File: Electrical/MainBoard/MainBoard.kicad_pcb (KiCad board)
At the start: 4 copper layers, 100 x 100 mm, 147 parts, among them J1 SNAP Program, J10 Refl_Mount, J11 Refl_Mount, J12 Refl_PCB_Connect, J13 Refl_PCB_Connect, J14 Refl_PCB_Connect, J15 USB_B_Micro, J16 MEM2061-01-188-00-A, J17 GPIO, J2 UART Connect, J3 SPI/I2C Connect, J4 5V Supply, J5 3.3V Supply, J6 USB_B_Micro, J7 Battery1, J8 Battery1, J9 Refl_Mount, K1 QRE1113GR, K2 QRE1113GR, K3 QRE1113GR, M1 Motor_DC, M2 Motor_DC, SW1 Reset, SW10 User_Button, SW2 5V Bypass, SW3 All Power Switch, SW4 SW_SPST, SW5 SW_SPST, SW6 SW_SPST, SW7 SW_SPST, SW8 User_Button, SW9 User_Button, U1 PIC32MZ2048EFH144-I/PL, U10 MCP2221A-I_SL, U11 M95M01-DFMN6TP, U12 DRV8842PWPR, U13 Quad_Encoder, U14 Quad_Encoder, U15 DRV8842PWPR, U2 GSF7002DW, U3 GSF7002DW, U4 GSF7002DW, U5 AP2114HA-3.3TRG1, U6 ICM-42688-P, U7 MAX-M8C-0, U8 GSF7002DW, U9 AP2114HA-3.3TRG1

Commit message: Begin layout of pcb
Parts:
- added E1: APAE1590R2540AKDB1-T, RobotLibrary:XDCR_APAE1590R2540AKDB1-T, F.Cu at (132.5, 86.4)
- C13: value 10 uF -> 4.7 uF; footprint Capacitor_THT:CP_Radial_Tantal_D5.0mm_P2.50mm -> Capacitor_SMD:C_0805_2012Metric_Pad1.18x1.45mm_HandSolder
- C14: value 0.1 uF -> 4.7 uF
- C15: value 2.2 uF -> 10 uF; footprint Capacitor_SMD:C_0805_2012Metric_Pad1.18x1.45mm_HandSolder -> Capacitor_THT:CP_Radial_Tantal_D5.0mm_P2.50mm
- C18: value 4.7 uF -> 2.2 uF
- C19: value 4.7 uF -> 0.1 uF
- C20, C26: value 0.1 uF -> 0.47 uF
- C21, C29: value 0.1 uF -> 0.01 uF
- C23, C31: value 0.47 uF -> 0.1 uF
- C24, C32: value 0.01 uF -> 0.1 uF
- C25, C33: value 0.1 uF -> 100 uF; footprint Capacitor_SMD:C_0805_2012Metric_Pad1.18x1.45mm_HandSolder -> RobotLibrary:PCAP_8x10-ELECT_NCA-M
- C28, C36: value 100 uF -> 0.1 uF; footprint RobotLibrary:PCAP_8x10-ELECT_NCA-M -> Capacitor_SMD:C_0805_2012Metric_Pad1.18x1.45mm_HandSolder
- D1: value LED 2 -> ON
- D2: value LED 1 -> LED 2
- D3: value LED 4 -> LED 1
- D4: value LED 3 -> LED 4
- D5: value LED 6 -> LED 3
- D6: value LED 5 -> LED 6
- D7: value ON -> LED 5
- J12: value Refl_PCB_Connect -> Refl_Mount; footprint RobotLibrary:CONN3_22232031_MOL -> Connector_PinHeader_2.54mm:PinHeader_2x02_P2.54mm_Vertical
- J15: value USB_B_Micro -> Refl_PCB_Connect; footprint RobotLibrary:AMPHENOL_10118193-0001LF -> RobotLibrary:CONN3_22232031_MOL
- J16: value MEM2061-01-188-00-A -> GPIO; footprint RobotLibrary:MEM2061-01-188-00-A_GCT -> Connector_PinHeader_2.54mm:PinHeader_2x10_P2.54mm_Vertical
- J17: value GPIO -> MEM2061-01-188-00-A; footprint Connector_PinHeader_2.54mm:PinHeader_2x10_P2.54mm_Vertical -> RobotLibrary:MEM2061-01-188-00-A_GCT
- J2: value UART Connect -> 3.3V Supply; footprint Connector_PinHeader_2.54mm:PinHeader_2x06_P2.54mm_Vertical -> Connector_PinHeader_2.54mm:PinHeader_2x05_P2.54mm_Vertical
- J3: value SPI/I2C Connect -> 5V Supply; footprint Connector_PinHeader_2.54mm:PinHeader_2x09_P2.54mm_Vertical -> Connector_PinHeader_2.54mm:PinHeader_2x05_P2.54mm_Vertical
- J4: value 5V Supply -> USB_B_Micro; footprint Connector_PinHeader_2.54mm:PinHeader_2x05_P2.54mm_Vertical -> RobotLibrary:AMPHENOL_10118193-0001LF
- J5: value 3.3V Supply -> Battery1; footprint Connector_PinHeader_2.54mm:PinHeader_2x05_P2.54mm_Vertical -> RobotLibrary:CONN_1017514
- J6: value USB_B_Micro -> Battery1; footprint RobotLibrary:AMPHENOL_10118193-0001LF -> RobotLibrary:CONN_1017514
- J7: value Battery1 -> UART Connect; footprint RobotLibrary:CONN_1017514 -> Connector_PinHeader_2.54mm:PinHeader_2x06_P2.54mm_Vertical
- J8: value Battery1 -> SPI/I2C Connect; footprint RobotLibrary:CONN_1017514 -> Connector_PinHeader_2.54mm:PinHeader_2x09_P2.54mm_Vertical
- J9: value Refl_Mount -> USB_B_Micro; footprint Connector_PinHeader_2.54mm:PinHeader_2x02_P2.54mm_Vertical -> RobotLibrary:AMPHENOL_10118193-0001LF
- R1: value 1k -> 10k
- R10, R11, R15, R16: value 1k -> 130R
- R17: value 130R -> 10k
- R18: value 130R -> 16k
- R19: value 100R -> 51k; moved to F.Cu
- R2, R37: value 10k -> 1k
- R20, R22, R24: value 10k -> 0R; moved to F.Cu
- R21, R23: value 100R -> 0R; moved to F.Cu
- R25: value 130R -> 1M
- R26: value 130R -> 0.25R
- R38: value 16k -> 1k
- R39: value 51k -> 1k
- R40: value 0R -> 1k
- R41: value 0R -> 100R; moved to B.Cu
- R42, R43: value 0R -> 100R
- R44: value 0R -> 10k; moved to B.Cu
- R45: value 1M -> 10k
- R46: value 0.25R -> 10k
- SW10, SW8, SW9: value User_Button -> SW_SPST
- SW4, SW5, SW6: value SW_SPST -> User_Button
- U10: value MCP2221A-I_SL -> DRV8842PWPR; footprint RobotLibrary:SOIC127P600X175-14N -> RobotLibrary:PWP0028C_M
- U11: value M95M01-DFMN6TP -> Quad_Encoder; footprint RobotLibrary:SO8N_4X5X1P27_STM-M -> RobotLibrary:CONN_22-23-2041_MOL
- U12: value DRV8842PWPR -> Quad_Encoder; footprint RobotLibrary:PWP0028C_M -> RobotLibrary:CONN_22-23-2041_MOL
- U13: value Quad_Encoder -> DRV8842PWPR; footprint RobotLibrary:CONN_22-23-2041_MOL -> RobotLibrary:PWP0028C_M
- U14: value Quad_Encoder -> MAX-M8C-0; footprint RobotLibrary:CONN_22-23-2041_MOL -> RobotLibrary:XCVR_MAX-M8C-0
- U15: value DRV8842PWPR -> M95M01-DFMN6TP; footprint RobotLibrary:PWP0028C_M -> RobotLibrary:SO8N_4X5X1P27_STM-M
- U2, U3: value GSF7002DW -> AP2114HA-3.3TRG1; footprint Package_TO_SOT_SMD:SOT-363_SC-70-6 -> RobotLibrary:SOT-223_DIO-M
- U4: value GSF7002DW -> ICM-42688-P; footprint Package_TO_SOT_SMD:SOT-363_SC-70-6 -> RobotLibrary:LGA14_2P5X3X0P91_TDK-M
- U5: value AP2114HA-3.3TRG1 -> GSF7002DW; footprint RobotLibrary:SOT-223_DIO-M -> Package_TO_SOT_SMD:SOT-363_SC-70-6
- U6: value ICM-42688-P -> GSF7002DW; footprint RobotLibrary:LGA14_2P5X3X0P91_TDK-M -> Package_TO_SOT_SMD:SOT-363_SC-70-6
- U7: value MAX-M8C-0 -> GSF7002DW; footprint RobotLibrary:XCVR_MAX-M8C-0 -> Package_TO_SOT_SMD:SOT-363_SC-70-6
- U9: value AP2114HA-3.3TRG1 -> MCP2221A-I_SL; footprint RobotLibrary:SOT-223_DIO-M -> RobotLibrary:SOIC127P600X175-14N
- moved M2 150.1 mm to (260.1, 127.6), turned to -90 degrees
- moved R35 138.6 mm to (260.3, 141.8), turned to -90 degrees
- moved R29 134.0 mm to (253.5, 131.5), turned to 90 degrees
- moved R43 133.9 mm to (234.7, 180.5)
- moved R36 133.3 mm to (257.8, 136.5), turned to 180 degrees
- moved R28 133.1 mm to (251.4, 131.5), turned to -90 degrees
- moved R46 130.7 mm to (238.8, 180.5)
- moved U13 128.0 mm to (250.3, 139.0), turned to 180 degrees
- moved R27 127.5 mm to (244.2, 131.6), turned to 90 degrees
- moved R32 126.6 mm to (242.8, 142.3)
- moved R33 126.1 mm to (242.8, 144.3)
- moved R34 125.7 mm to (242.8, 146.4)
- moved R30 125.4 mm to (242.8, 138.3)
- moved C29 125.1 mm to (263.2, 141.9), turned to 90 degrees
- moved R31 125.0 mm to (242.8, 140.3)
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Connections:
- C1 pad 1: GND -> Net-(C1-Pad1)
- C1 pad 2: +3.3V -> GND
- C10 pad 1: Net-(C10-Pad1) -> GND
- C10 pad 2: GND -> +3.3V
- C12 pad 1: +3.3V -> +5V
- C13 pad 1: +5V -> +3.3V
- C14 pad 1: +3.3V -> Net-(J2-Pin_1)
- C15 pad 1: +3.3V -> +5V
- C18 pad 1: +5V -> +3.3V
- C19 pad 1: Net-(J5-Pin_1) -> +3.3V
- C2 pad 1: GND -> +3.3V
- C2 pad 2: +3.3V -> GND
- C20 pad 1: +3.3V -> Net-(U10-V3P3OUT)
- C21 pad 1: GND -> Net-(U10-CP1)
- C21 pad 2: +3.3V -> Net-(U10-CP2)
- C22 pad 1: GND -> Net-(U10-VCP)
- C22 pad 2: +3.3V -> Vdrive
- C23 pad 1: Net-(U12-V3P3OUT) -> Vdrive
- C24 pad 1: Net-(U12-CP1) -> Vdrive
- C24 pad 2: Net-(U12-CP2) -> GND
- C25 pad 1: Net-(U12-VCP) -> Vdrive
- C25 pad 2: Vdrive -> GND
- C26 pad 1: Vdrive -> Net-(U13-V3P3OUT)
- C27 pad 1: Vdrive -> +3.3V
- C28 pad 1: Vdrive -> +3.3V
- C29 pad 1: +3.3V -> Net-(U13-CP1)
- C29 pad 2: GND -> Net-(U13-CP2)
- C30 pad 1: +3.3V -> Net-(U13-VCP)
- C30 pad 2: GND -> Vdrive
- C31 pad 1: Net-(U15-V3P3OUT) -> Vdrive
- C32 pad 1: Net-(U15-CP1) -> Vdrive
- C32 pad 2: Net-(U15-CP2) -> GND
- C33 pad 1: Net-(U15-VCP) -> Vdrive
- C33 pad 2: Vdrive -> GND
- C34 pad 1: Vdrive -> +3.3V
- C35 pad 1: Vdrive -> GND
- C35 pad 2: GND -> +3.3V
- C36 pad 1: Vdrive -> GND
- C36 pad 2: GND -> +3.3V
- C4 pad 1: +3.3V -> GND
- C4 pad 2: GND -> +3.3V
- D1 pad 1: Net-(D1-K) -> GND
- D6 pad 1: unconnected-(D6-K-Pad1) -> Net-(D6-K)
- D7 pad 1: GND -> Net-(D7-K)
- F1 pad 2: Net-(J7-Pin_1) -> Net-(J5-Pin_1)
- J12 pad 1: +3.3V -> Net-(J12-Pin_1)
- J12 pad 2: GND -> Net-(J12-Pin_2)
- J12 pad 3: /Refl1 -> Net-(J12-Pin_3)
- J13 pad 3: /Refl2 -> /Refl1
- J14 pad 3: /Refl3 -> /Refl2
- J15 pad 1: unconnected-(J15-VBUS-Pad1) -> +3.3V
- J15 pad 2: Net-(J15-D-) -> GND
- J15 pad 3: Net-(J15-D+) -> /Refl3
- J16 pad 10: unconnected-(J16-CARD_DETECT-Pad10) -> /RH12
- J16 pad 11: GND -> /RK1
- J16 pad 12: GND -> /RH13
- J16 pad 9: unconnected-(J16-CARD_DETECT-Pad9) -> /RJ15
- J17 pad 10: /RH12 -> unconnected-(J17-CARD_DETECT-Pad10)
- J17 pad 11: /RK1 -> GND
- J17 pad 12: /RH13 -> GND
- J17 pad 9: /RJ15 -> unconnected-(J17-CARD_DETECT-Pad9)
- J2 pad 1: /U3TX -> Net-(J2-Pin_1)
- J2 pad 2: /U3RX -> GND
- J2 pad 3: GND -> Net-(J2-Pin_1)
- J2 pad 5: /U4TX -> Net-(J2-Pin_1)
- J2 pad 6: /U4RX -> GND
- J2 pad 7: /U5TX -> Net-(J2-Pin_1)
- J2 pad 8: /U5RX -> GND
- J2 pad 9: GND -> Net-(J2-Pin_1)
- J3 pad 1: /SCK2 -> +5V
- J3 pad 10: /SDI3 -> GND
- J3 pad 2: /SDO2 -> GND
- J3 pad 3: /SS2* -> +5V
- J3 pad 4: /SDI2 -> GND
- J3 pad 5: GND -> +5V
- J3 pad 7: /SCK3 -> +5V
- J3 pad 8: /SDO3 -> GND
- J3 pad 9: /SS3* -> +5V
- J4 pad 1: +5V -> Net-(J4-VBUS)
- J4 pad 2: GND -> unconnected-(J4-D--Pad2)
- J4 pad 3: +5V -> unconnected-(J4-D+-Pad3)
- J4 pad 4: GND -> unconnected-(J4-ID-Pad4)
- J4 pad 5: +5V -> GND
- J5 pad 2: GND -> Net-(J5-Pin_2)
- J6 pad 1: Net-(J6-VBUS) -> Net-(J5-Pin_2)
- J6 pad 2: unconnected-(J6-D--Pad2) -> GND
- J7 pad 1: Net-(J7-Pin_1) -> /U3TX
- J7 pad 2: Net-(J7-Pin_2) -> /U3RX
- J8 pad 1: Net-(J7-Pin_2) -> /SCK2
- J8 pad 2: GND -> /SDO2
- J9 pad 1: Net-(J9-Pin_1) -> unconnected-(J9-VBUS-Pad1)
- J9 pad 2: Net-(J9-Pin_2) -> Net-(J9-D-)
- J9 pad 3: Net-(J9-Pin_3) -> Net-(J9-D+)
- K1 pad 2: Net-(J9-Pin_2) -> Net-(J10-Pin_2)
- K1 pad 3: Net-(J9-Pin_3) -> Net-(J10-Pin_3)
- K1 pad 4: Net-(J9-Pin_2) -> Net-(J10-Pin_2)
- K2 pad 2: Net-(J10-Pin_2) -> Net-(J11-Pin_2)
- K2 pad 3: Net-(J10-Pin_3) -> Net-(J11-Pin_3)
- K2 pad 4: Net-(J10-Pin_2) -> Net-(J11-Pin_2)
- K3 pad 2: Net-(J11-Pin_2) -> Net-(J12-Pin_2)
- K3 pad 3: Net-(J11-Pin_3) -> Net-(J12-Pin_3)
- K3 pad 4: Net-(J11-Pin_2) -> Net-(J12-Pin_2)
- R1 pad 1: Net-(J1-Pin_6) -> Net-(C1-Pad1)
- R1 pad 2: Net-(C10-Pad1) -> +3.3V
- R10 pad 1: /Bump1 -> Net-(D8-A1)
- R10 pad 2: GND -> Net-(U8-S1)
- R11 pad 1: /Bump2 -> Net-(D8-A2)
- R11 pad 2: GND -> Net-(U8-S2)
- R12 pad 1: /Bump3 -> /Switch2
- R13 pad 1: /Bump4 -> /Switch3
- R15 pad 1: /Switch2 -> +3.3V
- R15 pad 2: GND -> Net-(D9-A)
- R16 pad 1: /Switch3 -> +3.3V
- R16 pad 2: GND -> Net-(D10-A)
- R17 pad 1: Net-(D8-A2) -> /Fault1
- R17 pad 2: Net-(U8-S2) -> Net-(U10-V3P3OUT)
- R18 pad 1: Net-(D8-A1) -> Net-(U10-V3P3OUT)
- R18 pad 2: Net-(U8-S1) -> Net-(R18-Pad2)
- R19 pad 1: Net-(K1-Pad1) -> Net-(R18-Pad2)
- R19 pad 2: Net-(J9-Pin_1) -> GND
- R2 pad 1: Net-(C10-Pad1) -> Net-(J1-Pin_6)
- R2 pad 2: +3.3V -> Net-(C1-Pad1)
- R20 pad 1: Net-(J9-Pin_3) -> +3.3V
- R20 pad 2: Net-(J9-Pin_1) -> Net-(U10-I0)
- R21 pad 1: Net-(K2-Pad1) -> +3.3V
- R21 pad 2: Net-(J10-Pin_1) -> Net-(U10-I1)
- R22 pad 1: Net-(J10-Pin_3) -> +3.3V
- R22 pad 2: Net-(J10-Pin_1) -> Net-(U10-I2)
- R23 pad 1: Net-(K3-Pad1) -> +3.3V
- R23 pad 2: Net-(J11-Pin_1) -> Net-(U10-I3)
- R24 pad 1: Net-(J11-Pin_3) -> +3.3V
- R24 pad 2: Net-(J11-Pin_1) -> Net-(U10-I4)
- R25 pad 1: +3.3V -> Vdrive
- R25 pad 2: Net-(D9-A) -> Net-(U10-VCP)
- R26 pad 1: +3.3V -> GND
- R26 pad 2: Net-(D10-A) -> /MotorCurrent1
- R27 pad 1: /Fault1 -> /Fault2
- R27 pad 2: Net-(U12-V3P3OUT) -> Net-(U13-V3P3OUT)
- R28 pad 1: Net-(U12-V3P3OUT) -> Net-(U13-V3P3OUT)
- R30 pad 2: Net-(U12-I0) -> Net-(U13-I0)
- R31 pad 2: Net-(U12-I1) -> Net-(U13-I1)
- R32 pad 2: Net-(U12-I2) -> Net-(U13-I2)
- R33 pad 2: Net-(U12-I3) -> Net-(U13-I3)
- R34 pad 2: Net-(U12-I4) -> Net-(U13-I4)
- R35 pad 2: Net-(U12-VCP) -> Net-(U13-VCP)
- R36 pad 2: /MotorCurrent1 -> /MotorCurrent2
- R37 pad 1: /Fault2 -> /Bump1
- R37 pad 2: Net-(U15-V3P3OUT) -> GND
- R38 pad 1: Net-(U15-V3P3OUT) -> /Bump2
- R38 pad 2: Net-(R38-Pad2) -> GND
- R39 pad 1: Net-(R38-Pad2) -> /Bump3
- R40 pad 1: +3.3V -> /Bump4
- R40 pad 2: Net-(U15-I0) -> GND
- R41 pad 1: +3.3V -> Net-(K1-Pad1)
- R41 pad 2: Net-(U15-I1) -> Net-(J10-Pin_1)
- R42 pad 1: +3.3V -> Net-(K2-Pad1)
- R42 pad 2: Net-(U15-I2) -> Net-(J11-Pin_1)
- R43 pad 1: +3.3V -> Net-(K3-Pad1)
- R43 pad 2: Net-(U15-I3) -> Net-(J12-Pin_1)
- R44 pad 1: +3.3V -> Net-(J10-Pin_3)
- R44 pad 2: Net-(U15-I4) -> Net-(J10-Pin_1)
- R45 pad 1: Vdrive -> Net-(J11-Pin_3)
- R45 pad 2: Net-(U15-VCP) -> Net-(J11-Pin_1)
- R46 pad 1: GND -> Net-(J12-Pin_3)
- R46 pad 2: /MotorCurrent2 -> Net-(J12-Pin_1)
- SW1 pad 4: Net-(C10-Pad1) -> Net-(C1-Pad1)
- SW10 pad 2: /Switch3 -> /Bump4
- SW2 pad 1: Net-(J6-VBUS) -> Net-(J4-VBUS)
- SW3 pad 2: Net-(J6-VBUS) -> Net-(J4-VBUS)
- SW4 pad 2: /Bump1 -> /Switch2
- SW5 pad 2: /Bump2 -> /Switch3
- SW6 pad 2: /Bump3 -> /Switch1
- SW7 pad 2: /Bump4 -> /Bump1
- SW8 pad 2: /Switch1 -> /Bump2
- SW9 pad 2: /Switch2 -> /Bump3
- U1 pad 65: /LED1 -> /LED2
- U1 pad 66: /LED2 -> /LED1
- U1 pad 67: /LED3 -> /LED4
- U1 pad 68: /LED4 -> /LED3
- U1 pad 71: /LED5 -> /LED6
- U1 pad 72: /LED6 -> /LED5
- U10 pad 1: +3.3V -> Net-(U10-CP1)
- U10 pad 10: unconnected-(U10-SCL-Pad10) -> Net-(M1-+)
- U10 pad 11: +3.3V -> Vdrive
- U10 pad 12: Net-(J15-D-) -> Net-(R18-Pad2)
- U10 pad 13: Net-(J15-D+) -> Net-(R18-Pad2)
- U10 pad 2: Net-(D10-K) -> Net-(U10-CP2)
- U10 pad 3: Net-(D9-K) -> Net-(U10-VCP)
- U10 pad 4: /USB_RST -> Vdrive
- U10 pad 5: /U1TX -> Net-(M1-+)
- U10 pad 6: /U1RX -> /MotorCurrent1
- U10 pad 7: unconnected-(U10-GP2-Pad7) -> Net-(M1--)
- U10 pad 8: unconnected-(U10-GP3-Pad8) -> Net-(M1--)
- U10 pad 9: unconnected-(U10-SDA-Pad9) -> /MotorCurrent1
- U11 pad 1: /SS5* -> /IC3
- U11 pad 2: /SDI5 -> /IC4
- U11 pad 3: /Write Protect* -> +3.3V
- U12 pad 1: Net-(U12-CP1) -> /IC1
- U12 pad 2: Net-(U12-CP2) -> /IC2
- U12 pad 3: Net-(U12-VCP) -> +3.3V
- U12 pad 4: Vdrive -> GND
- U13 pad 1: /IC1 -> Net-(U13-CP1)
- U13 pad 2: /IC2 -> Net-(U13-CP2)
- U13 pad 3: +3.3V -> Net-(U13-VCP)
- U13 pad 4: GND -> Vdrive
- U14 pad 1: /IC3 -> GND
- U14 pad 2: /IC4 -> /U2RX
- U14 pad 3: +3.3V -> /U2TX
- U14 pad 4: GND -> unconnected-(U14-TIMEPULSE-Pad4)
- U15 pad 1: Net-(U15-CP1) -> /SS5*
- U15 pad 2: Net-(U15-CP2) -> /SDI5
- U15 pad 3: Net-(U15-VCP) -> /Write Protect*
- U15 pad 4: Vdrive -> GND
- U15 pad 5: Net-(M2-+) -> /SDO5
- U15 pad 6: /MotorCurrent2 -> /SCK5
- U15 pad 7: Net-(M2--) -> /Hold*
- U15 pad 8: Net-(M2--) -> +3.3V
- U2 pad 1: GND -> +5V
- U2 pad 2: /LED6 -> GND
- U2 pad 3: Net-(D1-K) -> +3.3V
- U3 pad 1: GND -> +5V
- U3 pad 2: /LED4 -> GND
- U3 pad 3: Net-(D3-K) -> Net-(J2-Pin_1)
- U4 pad 1: unconnected-(U4-S1-Pad1) -> /SDI1
- U4 pad 2: unconnected-(U4-G1-Pad2) -> GND
- U4 pad 3: unconnected-(U4-D2-Pad3) -> GND
- U4 pad 4: Net-(D5-K) -> /IMU_INT1
- U4 pad 5: /LED2 -> +3.3V
- U4 pad 6: unconnected-(U4-D1-Pad6) -> GND
- U5 pad 1: +5V -> GND
- U5 pad 2: GND -> /LED1
- U5 pad 3: +3.3V -> Net-(D2-K)
- U6 pad 1: /SDI1 -> GND
- U6 pad 2: GND -> /LED3
- U6 pad 3: GND -> Net-(D4-K)
- U6 pad 4: /IMU_INT1 -> GND
- U6 pad 5: +3.3V -> /LED4
- U6 pad 6: GND -> Net-(D5-K)
- U7 pad 2: /U2RX -> /LED5
- U7 pad 3: /U2TX -> Net-(D6-K)
- U7 pad 4: unconnected-(U7-TIMEPULSE-Pad4) -> GND
- U7 pad 5: /GPS_INT -> /LED6
- U7 pad 6: unconnected-(U7-V_BCKP-Pad6) -> Net-(D7-K)
- U9 pad 1: +5V -> +3.3V
- U9 pad 2: GND -> Net-(D10-K)
- U9 pad 3: Net-(J5-Pin_1) -> Net-(D9-K)
- U9 pad 4: GND -> /USB_RST
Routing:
- net /SDI6: track 0.00 -> 72.4 mm, vias 0 -> 2
- net Vdrive: track 0.00 -> 72.3 mm
- net +3.3V: track 74.8 -> 143.1 mm, vias 19 -> 33
- net /SDO6: track 0.00 -> 67.1 mm, vias 0 -> 2
- net /U1RX: track 0.00 -> 56.7 mm
- net /USB_RST: track 0.00 -> 53.6 mm
- net /U1TX: track 0.00 -> 49.3 mm
- net /SCK6: track 0.00 -> 45.4 mm, vias 0 -> 2
- net Net-(J2-Pin_1): track 0.00 -> 45.1 mm
- net GND: track 60.1 -> 104.4 mm, vias 29 -> 52
- net /SS6*: track 0.00 -> 42.0 mm, vias 0 -> 2
- net Net-(F1-Pad1): track 50.0 -> 21.9 mm
- net Net-(J7-Pin_2): track 25.9 -> 0.00 mm
- net Net-(J4-VBUS): track 0.00 -> 25.4 mm
- net Net-(J6-VBUS): track 25.2 -> 0.00 mm
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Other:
- outline, holes or cut-outs redrawn
- board text added: "G"
- board text added: "RX"
- board text added: "S"
- board text added: "TX"
- board text added: "V"
- board text added: "x"

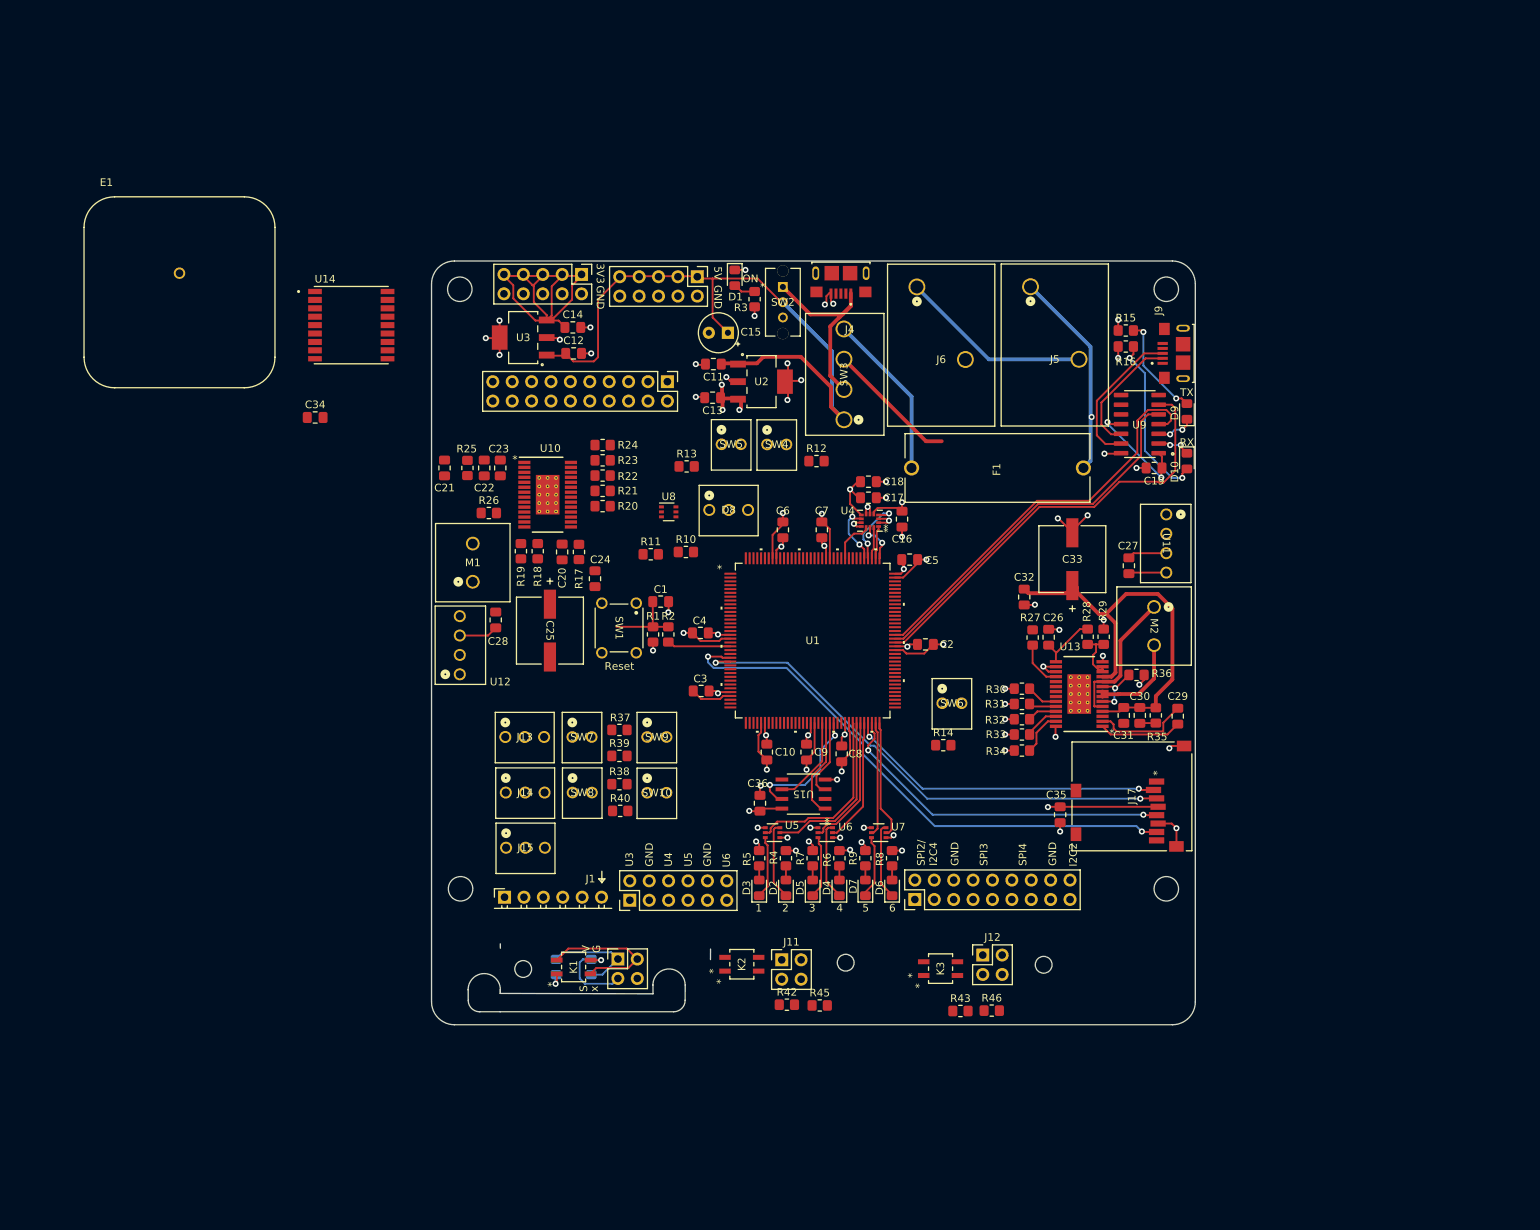
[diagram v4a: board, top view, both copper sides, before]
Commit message: First Pass at the routing
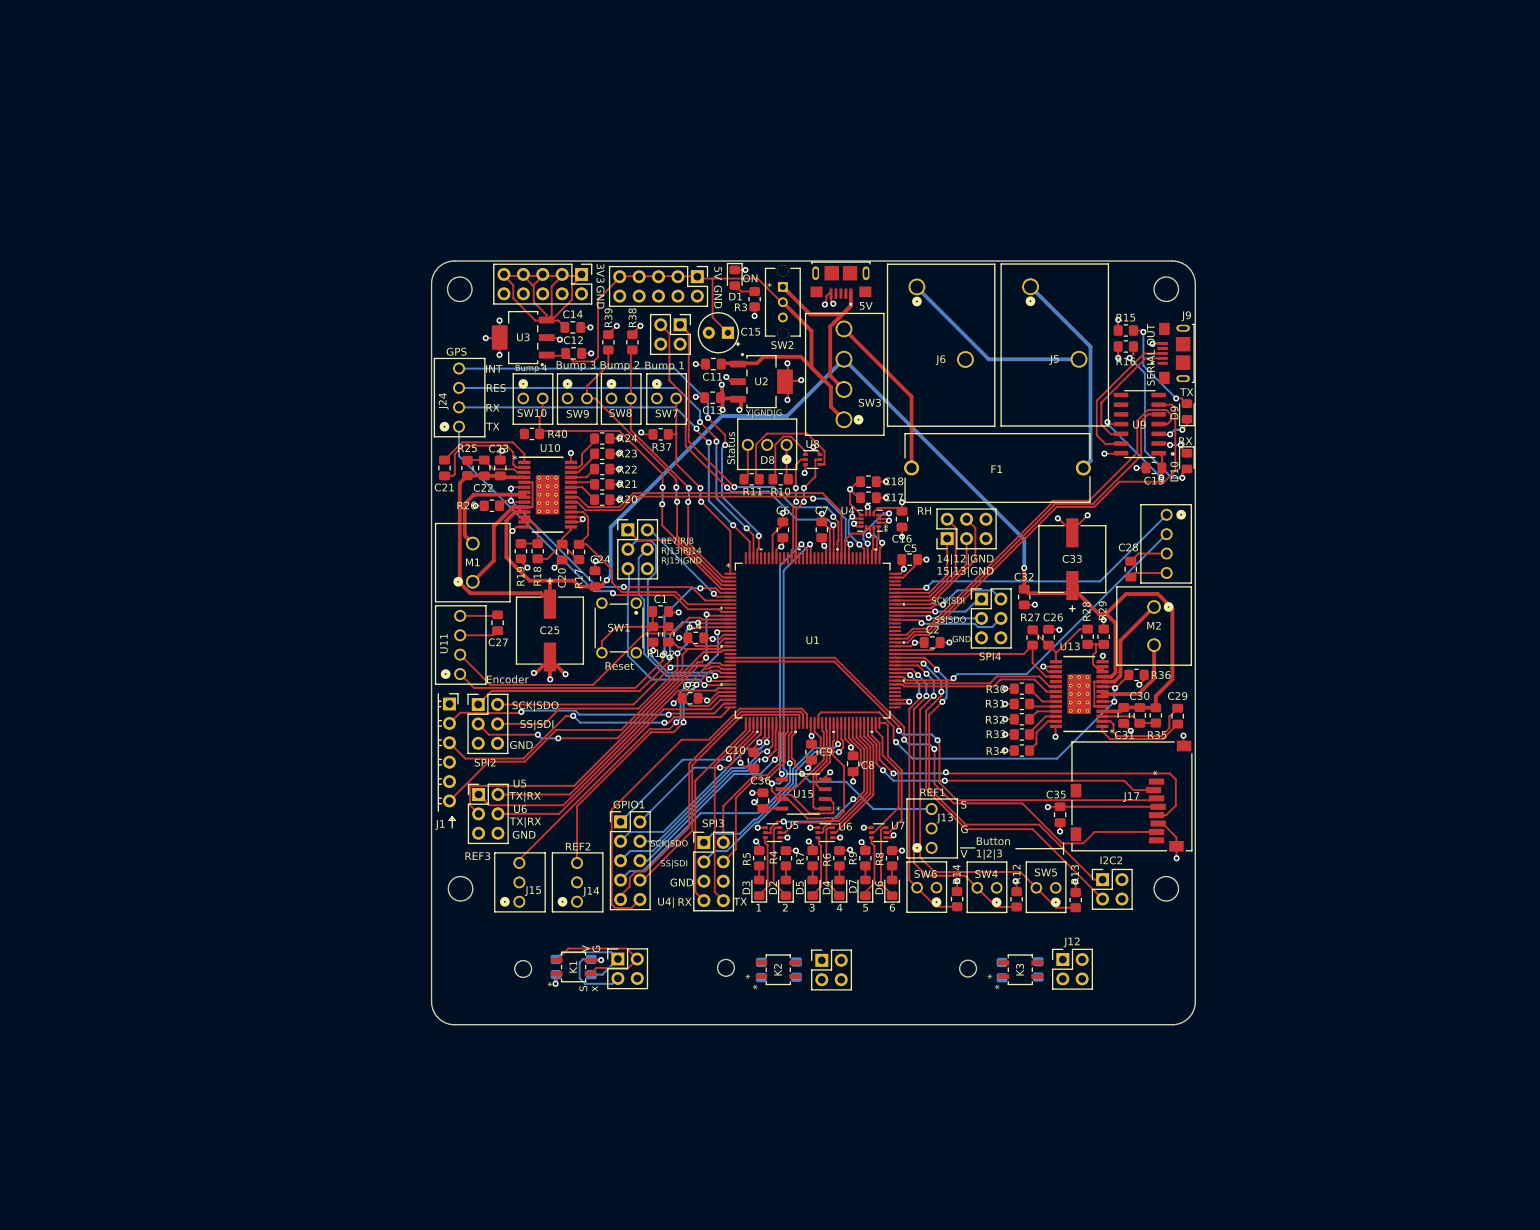
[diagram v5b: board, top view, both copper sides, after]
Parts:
- removed C34: 0.1 uF, Capacitor_SMD:C_0805_2012Metric_Pad1.18x1.45mm_HandSolder
- removed E1: APAE1590R2540AKDB1-T, RobotLibrary:XDCR_APAE1590R2540AKDB1-T
- removed U14: MAX-M8C-0, RobotLibrary:XCVR_MAX-M8C-0
- added J18: Conn_02x02_Odd_Even, Connector_PinHeader_2.54mm:PinHeader_2x02_P2.54mm_Vertical, F.Cu at (253.4, 163.3)
- added J19: Conn_02x03_Odd_Even, Connector_PinHeader_2.54mm:PinHeader_2x03_P2.54mm_Vertical, F.Cu at (237.5, 126.6)
- added J20: Conn_02x03_Odd_Even, Connector_PinHeader_2.54mm:PinHeader_2x03_P2.54mm_Vertical, F.Cu at (171.6, 140.4)
- added J21: Conn_02x03_Odd_Even, Connector_PinHeader_2.54mm:PinHeader_2x03_P2.54mm_Vertical, F.Cu at (233.0, 118.7)
- added J22: Conn_02x02_Odd_Even, Connector_PinHeader_2.54mm:PinHeader_2x02_P2.54mm_Vertical, F.Cu at (198.1, 90.7)
- added J23: Conn_02x03_Odd_Even, Connector_PinHeader_2.54mm:PinHeader_2x03_P2.54mm_Vertical, F.Cu at (171.7, 152.2)
- added J24: Conn_01x04, RobotLibrary:CONN_22-23-2041_MOL, F.Cu at (169.1, 104.0)
- J16: value GPIO -> Conn_02x03_Odd_Even; footprint Connector_PinHeader_2.54mm:PinHeader_2x10_P2.54mm_Vertical -> Connector_PinHeader_2.54mm:PinHeader_2x03_P2.54mm_Vertical
- J7: value UART Connect -> GPIO1; footprint Connector_PinHeader_2.54mm:PinHeader_2x06_P2.54mm_Vertical -> Connector_PinHeader_2.54mm:PinHeader_2x05_P2.54mm_Vertical
- J8: value SPI/I2C Connect -> Conn_02x04_Odd_Even; footprint Connector_PinHeader_2.54mm:PinHeader_2x09_P2.54mm_Vertical -> Connector_PinHeader_2.54mm:PinHeader_2x04_P2.54mm_Vertical
- R42, R43, R45, R46: moved to B.Cu
- moved U12 94.9 mm to (261.8, 115.5), turned to -90 degrees
- moved U11 94.8 mm to (169.2, 136.4), turned to 90 degrees
- moved C28 83.4 mm to (257.1, 122.7), turned to -90 degrees
- moved C27 83.0 mm to (174.2, 129.7), turned to 90 degrees
- moved R13 76.3 mm to (249.8, 166.0), turned to 90 degrees
- moved SW5 72.7 mm to (247.2, 164.4), turned to 180 degrees
- moved SW4 65.4 mm to (239.5, 164.4), turned to 180 degrees
- moved R12 63.1 mm to (242.1, 165.9), turned to 90 degrees
- moved R38 57.9 mm to (191.8, 93.0), turned to 90 degrees
- moved J13 57.7 mm to (231.0, 159.1), turned to 90 degrees
- moved R39 54.2 mm to (188.7, 93.0), turned to 90 degrees
- moved SW10 54.1 mm to (177.5, 100.3)
- moved SW8 51.9 mm to (189.1, 100.3)
- moved R40 50.7 mm to (178.7, 105.0), turned to 180 degrees
- moved SW7 45.7 mm to (195.0, 100.3)
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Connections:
- J16 pad 1: /RB4 -> /RE7
- J16 pad 2: /RH0 -> /RJ8
- J16 pad 3: /RJ11 -> /RJ13
- J16 pad 4: /RH1 -> /RJ14
- J16 pad 5: /RJ13 -> /RJ15
- J16 pad 6: /RH2 -> GND
- J7 pad 1: /U3TX -> /RA9
- J7 pad 10: GND -> /RK3
- J7 pad 2: /U3RX -> /RA10
- J7 pad 3: GND -> /RH0
- J7 pad 4: GND -> /RH1
- J7 pad 5: /U4TX -> /RH2
- J7 pad 6: /U4RX -> /RH3
- J7 pad 7: /U5TX -> /RB10
- J7 pad 8: /U5RX -> /RK1
- J7 pad 9: GND -> /RK2
- J8 pad 1: /SCK2 -> /SCK3
- J8 pad 2: /SDO2 -> /SDO3
- J8 pad 3: /SS2* -> /SS3*
- J8 pad 4: /SDI2 -> /SDI3
- J8 pad 7: /SCK3 -> /U4RX
- J8 pad 8: /SDO3 -> /U4TX
- U1 pad 10: /Fault2 -> unconnected-(U1A-EBIBS1/RJ10-Pad10)
- U1 pad 26: /RB4 -> /Refl3
- U1 pad 27: /RJ11 -> /Refl2
- U1 pad 5: /Refl1 -> /RE7
- U1 pad 50: /RB11 -> /Refl1
- U1 pad 6: /Refl2 -> /IC3
- U1 pad 7: /Refl3 -> /RJ8
- U1 pad 87: unconnected-(U1B-EBIA14/PMCS1/PMA14/RA4-Pad87) -> /Fault2
- U1 pad 95: /IC3 -> unconnected-(U1B-RPA14/SCL1/RA14-Pad95)
- U10 pad 20: /Dir1 -> /Dir2
- U10 pad 21: /OC1 -> /OC2
- U13 pad 20: /Dir2 -> /Dir1
- U13 pad 21: /OC2 -> /OC1
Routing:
- net Vdrive: track 72.3 -> 201.8 mm, vias 0 -> 2
- net /GPS_INT: track 0.00 -> 58.1 mm, vias 0 -> 3
- net /GPS_Reset: track 0.00 -> 55.0 mm, vias 0 -> 3
- net /Switch3: track 0.00 -> 52.9 mm, vias 0 -> 2
- net /U2RX: track 0.00 -> 52.1 mm, vias 0 -> 3
- net /SCL2: track 0.00 -> 51.2 mm, vias 0 -> 2
- net /U6TX: track 0.00 -> 50.9 mm, vias 0 -> 2
- net /SDA2: track 0.00 -> 50.8 mm, vias 0 -> 2
- net /SDI5: track 0.00 -> 49.3 mm, vias 0 -> 2
- net /RK3: track 0.00 -> 49.3 mm
- net /U2TX: track 0.00 -> 47.8 mm, vias 0 -> 1
- net /MotorCurrent2: track 7.62 -> 54.1 mm, vias 2 -> 3
- net /U3RX: track 0.00 -> 45.3 mm, vias 0 -> 2
- net /IC3: track 0.00 -> 45.1 mm, vias 0 -> 2
- net /Switch2: track 0.00 -> 44.9 mm, vias 0 -> 2
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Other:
- outline, holes or cut-outs redrawn
- board text added: "14|12|GND 15|13|GND"
- board text added: "Bump 1"
- board text added: "Bump 2"
- board text added: "Bump 3"
- board text added: "Bump 4"
- board text added: "Button 1|2|3"
- board text added: "Encoder"
- board text added: "GPIO1"
- board text added: "GPS"
- board text added: "INT"
- board text added: "RE7|RJ8 RJ13|RJ14 RJ15|GND"
- board text added: "REF1"
- board text added: "REF2"
- board text added: "REF3"
- board text added: "RES"
- board text added: "RH"
- board text added: "S G V"
- board text added: "SCK|SDI"
- board text added: "SCK|SDO"
- board text added: "SERIAL OUT"
- board text added: "SPI2"
- board text added: "SS|SDI"
- board text added: "SS|SDO"
- board text added: "Status"
- board text added: "U4|"
- board text added: "U5 TX|RX"
- board text added: "U6 TX|RX"
- board text added: "Y|GND|G"
- board text removed: "SPI2/ I2C4"
- board text removed: "U3"
- board text removed: "U4"
- board text removed: "U5"
- board text removed: "U6"

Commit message: Add some finishing touches and create preliminary boms
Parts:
- C16: value 10 nF -> 0.01 uF
- D1: value ON -> LED
- D2: value LED 2 -> LED
- D3: value LED 1 -> LED
- D4: value LED 4 -> LED
- D5: value LED 3 -> LED
- D6: value LED 6 -> LED
- D7: value LED 5 -> LED
- moved J11 5.51 mm to (222.1, 173.7)
- moved H6 5.51 mm to (209.6, 174.7)
- moved K2 5.51 mm to (216.4, 175.0)
- moved R42 5.51 mm to (214.2, 175.0), turned to 90 degrees
- moved R45 5.51 mm to (218.8, 174.9)
- moved R46 3.24 mm to (248.2, 175.0)
- moved J12 3.19 mm to (251.3, 173.7)
- moved K3 3.08 mm to (245.7, 174.9)
- moved H7 3.07 mm to (238.8, 174.9)
- moved R43 2.95 mm to (243.1, 174.9), turned to 90 degrees
- moved H5 1.35 mm to (178.8, 174.9)
- moved K1 1.35 mm to (185.4, 174.7)
- moved R41 1.35 mm to (183.2, 174.7)
- moved R44 1.35 mm to (187.8, 174.7)
- moved J10 1.35 mm to (191.2, 173.7)
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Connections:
- C22 pad 1: Net-(U10-VCP) -> Vdrive
- C22 pad 2: Vdrive -> Net-(U10-VCP)
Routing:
- net Net-(J11-Pin_2): track 0.00 -> 18.4 mm
- net Net-(J12-Pin_2): track 0.00 -> 18.4 mm
- net Net-(J11-Pin_1): track 0.00 -> 13.1 mm
- net Net-(J12-Pin_1): track 0.00 -> 12.9 mm
- net Net-(J11-Pin_3): track 0.00 -> 11.2 mm, vias 0 -> 1
- net Net-(J12-Pin_3): track 0.00 -> 10.8 mm, vias 0 -> 1
- net Net-(K3-Pad1): track 0.00 -> 2.59 mm, vias 0 -> 1
- net Net-(K2-Pad1): track 0.00 -> 2.49 mm, vias 0 -> 1
- net GND: track 147.9 -> 149.2 mm, vias 71 -> 72
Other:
- outline, holes or cut-outs redrawn
- board text added: "locked"
- board text removed: "G"
- board text removed: "S"
- board text removed: "V"
- board text removed: "x"

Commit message: Some finishing touches to the board
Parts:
- moved J6 16.6 mm to (235.5, 101.0), turned to 180 degrees
- moved J5 16.5 mm to (250.1, 101.0), turned to 180 degrees
- moved M1 5.25 mm to (171.0, 119.0), turned to -90 degrees
- moved M2 5.15 mm to (260.1, 132.8), turned to 90 degrees
- moved J15 0.47 mm to (177.4, 166.3)
- moved J14 0.23 mm to (184.7, 166.4)
- turned C22 to 90 degrees
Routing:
- net Net-(J5-Pin_1): track 27.4 -> 7.65 mm
- net Net-(J5-Pin_2): track 25.1 -> 12.9 mm
- net Net-(M2--): track 12.7 -> 19.0 mm
- net Net-(M1-+): track 18.8 -> 13.2 mm
- net Net-(M1--): track 14.6 -> 19.9 mm
- net Net-(M2-+): track 18.9 -> 14.5 mm
- net Vdrive: track 201.8 -> 203.9 mm
- net Net-(J11-Pin_1): track 13.1 -> 11.4 mm
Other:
- board text added: "-/+"
- board text added: "G"
- board text added: "Hole Spacing: 92.5 mm x 78.5 mm Board Size: 100 mm x 86.5 mm Hole Size: M3"
- board text added: "Main Power Switch"
- board text added: "Matthew Sato Engineering Informatics Group Stanford University Robot Control, Rev 0.1 11/24/2023"
- board text added: "Motor Controller, Encoder, IMU, EEPROM, Cliff Sensors, Bumpers, Buttons, USB, LED"
- board text added: "PIC32MZ2048EFH144-I/PL"
- board text added: "S"
- board text added: "V"
- board text added: "x"
